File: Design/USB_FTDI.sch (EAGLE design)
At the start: 24 parts, among them IC1 FT232RL-REEL, J1 USB1061-GF-L-A, U1 LM3940IMP-3.3

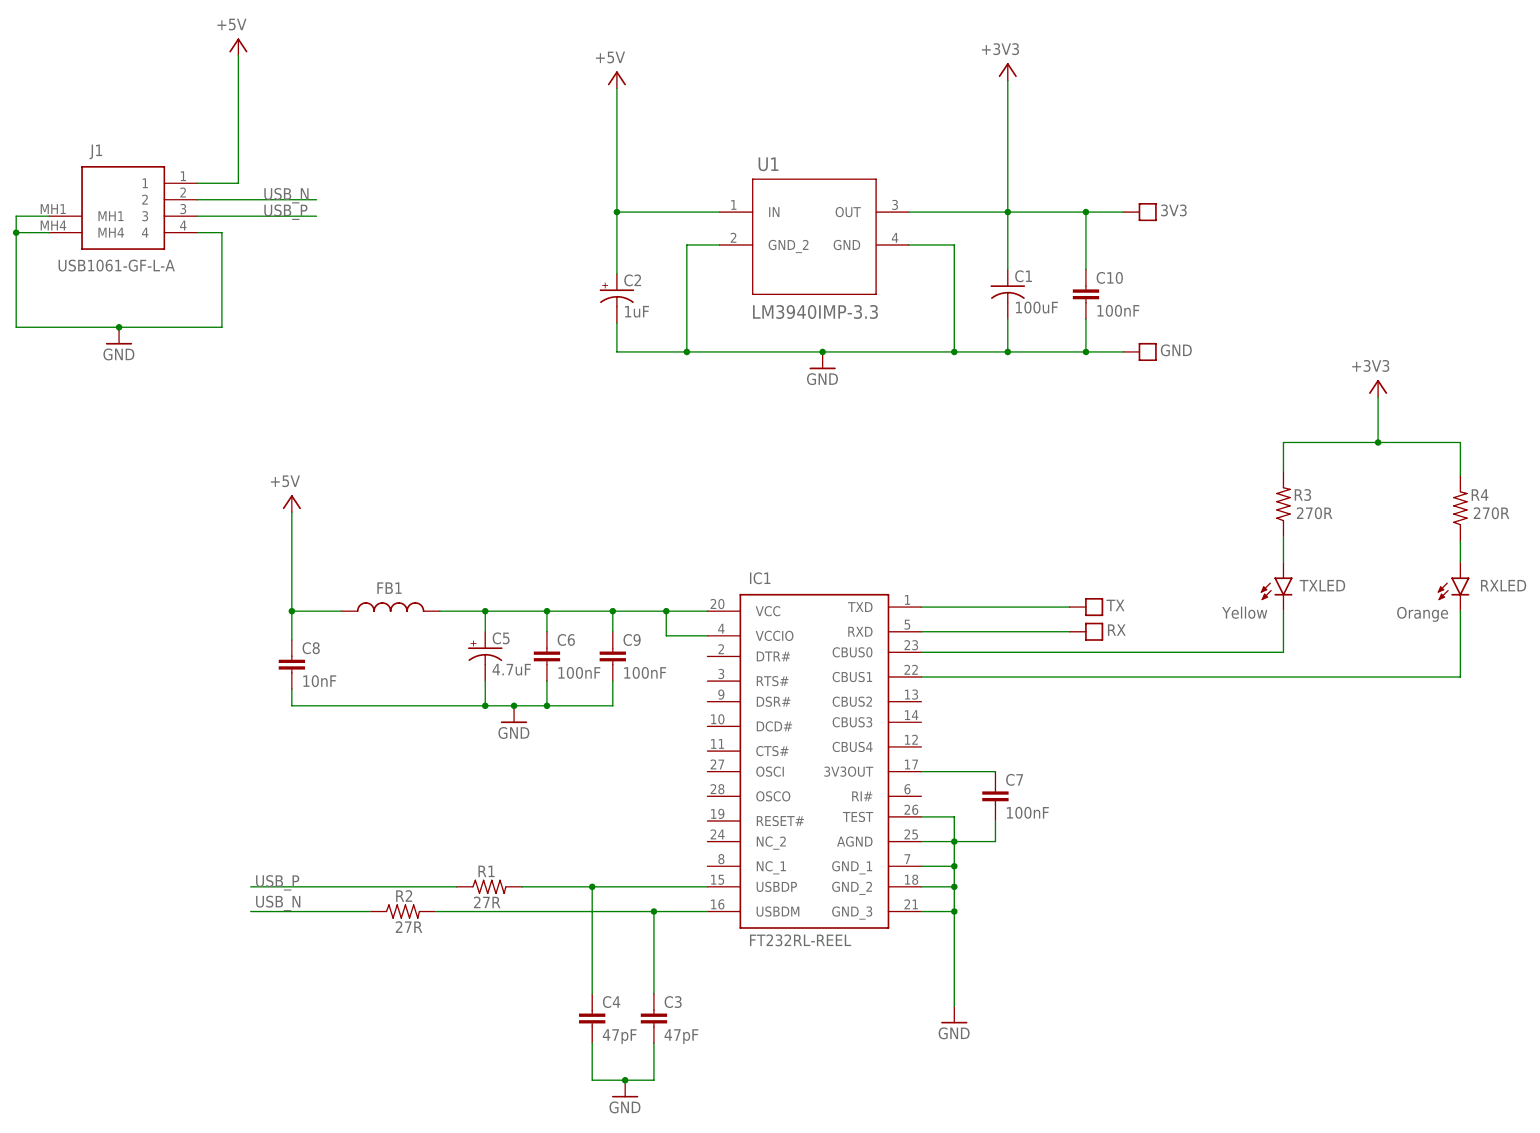
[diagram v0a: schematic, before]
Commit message: - Connect the VCCIO pin of the FTDI IC to the 3.3V - Improve the layout to offer better thermal conductivity for the LDO
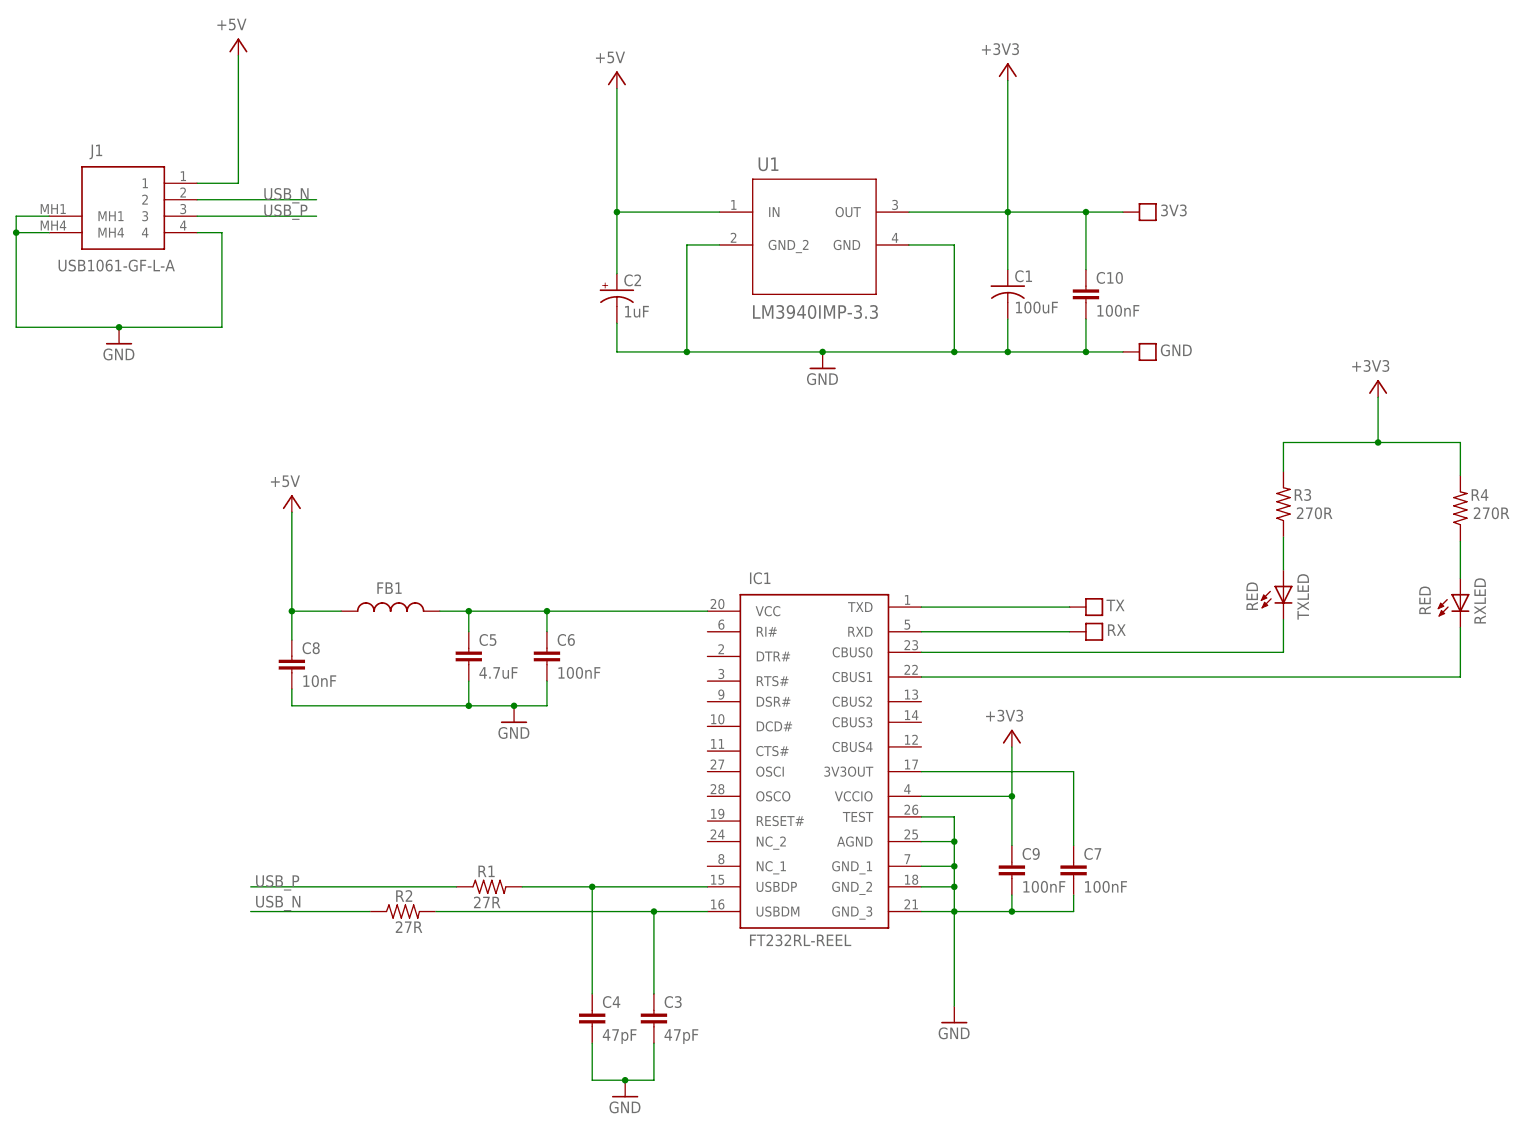
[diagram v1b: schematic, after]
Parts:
- C5: device HEXABITZ_RCLS:C-0805-POL -> HEXABITZ_RCLS:C-0805
- RXLED: value Orange -> RED; device HEXABITZ_USER_INTERFACE_PARTS:LEDCHIP-LED0805 -> HEXABITZ_USER_INTERFACE_PARTS:VLMS1300-GS08
- TXLED: value Yellow -> RED; device HEXABITZ_USER_INTERFACE_PARTS:LEDCHIP-LED0805 -> HEXABITZ_USER_INTERFACE_PARTS:VLMS1300-GS08
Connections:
- net +3V3: now also C9.1, IC1.VCCIO
- net GND: now also C5.2; no longer C5.-
- net N$5: now also C5.1; no longer C5.+, C9.1, IC1.VCCIO
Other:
- note removed: "0"
- note removed: "2"
- moved on the sheet: C7, C9
